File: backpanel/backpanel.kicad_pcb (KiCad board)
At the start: 2 copper layers, 158.8 x 44.4 mm, 8 parts

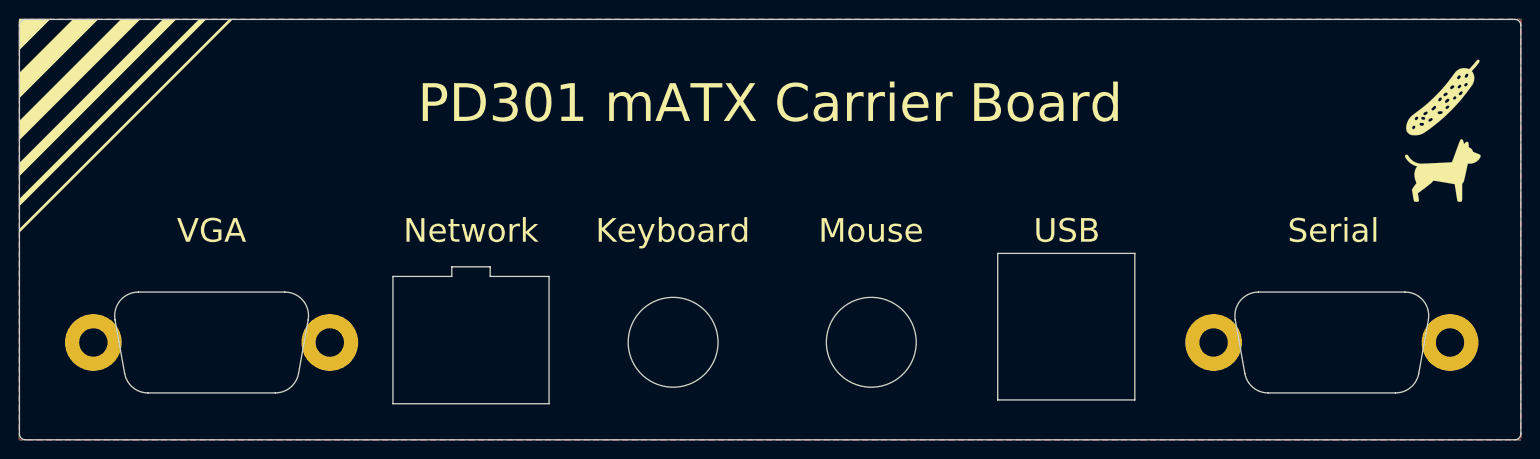
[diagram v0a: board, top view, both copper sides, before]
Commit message: Adjust backpanel design for better fit
Move Ethernet jack to be flush through backpanel, make per-port cutouts for USB
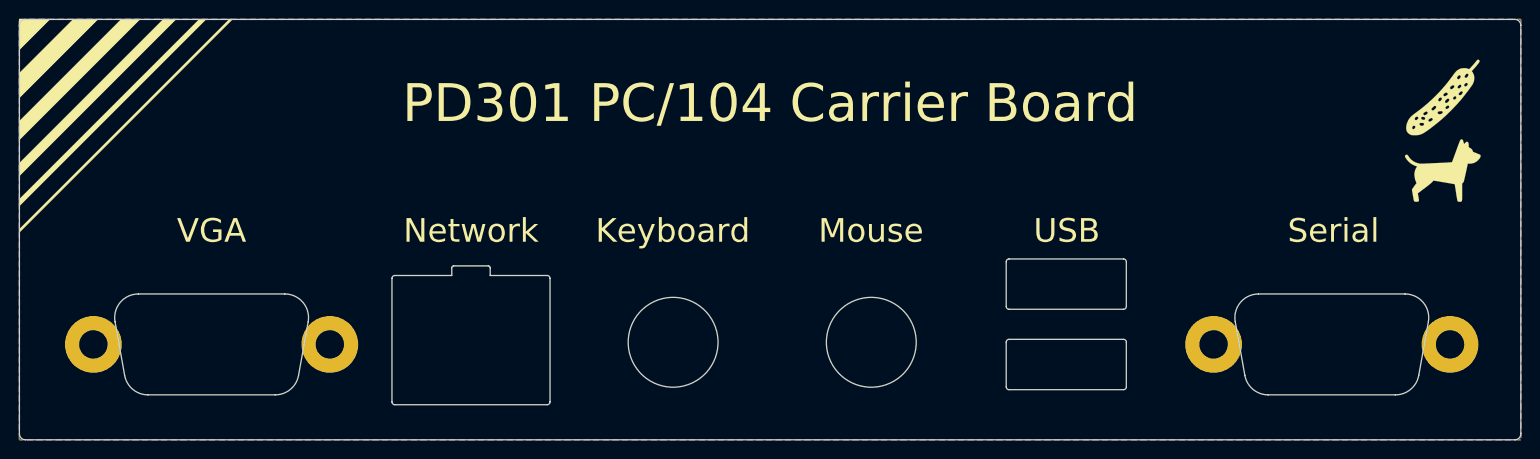
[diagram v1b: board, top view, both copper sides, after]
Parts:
- moved H1 0.20 mm to (33.2, 59.8)
- moved H2 0.20 mm to (58.2, 59.8)
- moved H3 0.20 mm to (151.7, 59.8)
- moved H4 0.20 mm to (176.7, 59.8)
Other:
- outline, holes or cut-outs redrawn
- board text added: "PD301 I/O Shield v1.1"
- board text added: "PD301 PC/104 Carrier Board"
- board text removed: "PD301 I/O Shield v1.0"
- board text removed: "PD301 mATX Carrier Board"
